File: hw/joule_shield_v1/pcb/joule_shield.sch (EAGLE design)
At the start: 143 parts, among them J1 MF-CON-MICROUSB-RIGHT, J4 USB_AUSB_A_SMT_RA, J5 JST-ZH5SMT_RA, J6 INTEL_JOULE_J6, J7 INTEL_JOULE_J7, J8 DM3ATDM3AT, Q1 NFETEMT3F, Q2 NFETEMT3F, Q3 NFETEMT3F, Q4 NFETEMT3F, Q5 NFETEMT3F, SW1 MF-SW-TACT-4.2MM, SW2 MF-SW-TACT-4.2MM, SW3 MF-SW-TACT-4.2MM, U1 BQ25892PWQFN-24, U10 FT231XQFN-20, U2 FAN8623WLCSP16, U3 TPS63201PVSON-14, U4 TLV62084PWSON-8, U5 TPS2553PWSON-6, U6 TPS2553PWSON-6, U7 SINGLE-BIT_BUS_TRANSCEIVER, U8 SINGLE-BIT_BUS_TRANSCEIVER, U9 SN74AVCA406L

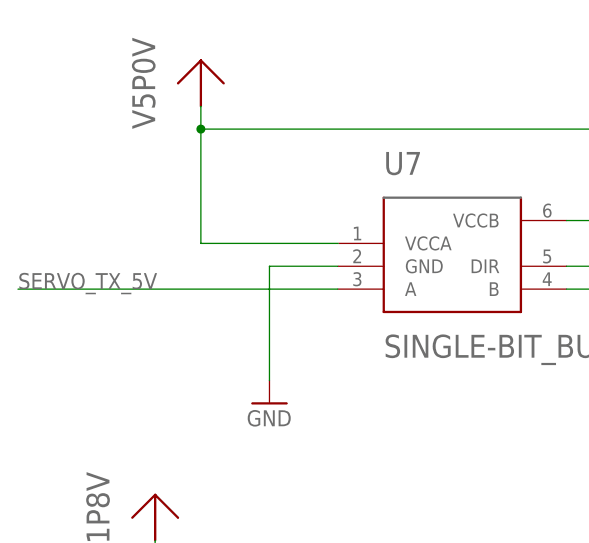
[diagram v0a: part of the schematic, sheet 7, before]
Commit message: joule shield: Do grounds for things up through the SD level converter.
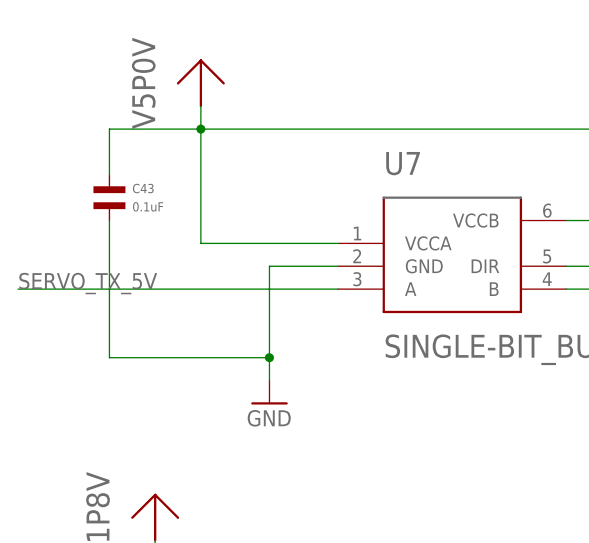
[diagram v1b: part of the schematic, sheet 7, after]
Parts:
- added C43: 0.1uF, mf_passives:CAPACITOR_NP_0603
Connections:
- net GND: now also C43.P$2
- net V5P0V: now also C43.P$1
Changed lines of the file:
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@@
 <part name="U$47" library="joule_shield" deviceset="VSYS" device=""/>
 <part name="U$13" library="joule_shield" deviceset="VSYS" device=""/>
+<part name="C43" library="mf_passives" deviceset="CAPACITOR_NP" device="_0603" value="0.1uF">
+<attribute name="MPN" value="MF-CAP-0603-0.1uF"/>
+</part>
 </parts>
 <sheets>
@@
 <instance part="C29" gate="G$1" x="25.4" y="27.94"/>
 <instance part="U$26" gate="G$1" x="96.52" y="91.44"/>
+<instance part="C43" gate="G$1" x="27.94" y="81.28"/>
 </instances>
 <busses>
@@
 <pinref part="U7" gate="G$1" pin="DIR"/>
 <wire x1="83.82" y1="73.66" x2="78.74" y2="73.66" width="0.1524" layer="91"/>
+<wire x1="38.1" y1="88.9" x2="27.94" y2="88.9" width="0.1524" layer="91"/>
+<pinref part="C43" gate="G$1" pin="P$1"/>
+<wire x1="27.94" y1="88.9" x2="27.94" y2="83.82" width="0.1524" layer="91"/>
 </segment>
 <segment>
@@
 <segment>
 <pinref part="GND24" gate="1" pin="GND"/>
-<wire x1="45.72" y1="60.96" x2="45.72" y2="73.66" width="0.1524" layer="91"/>
+<wire x1="45.72" y1="60.96" x2="45.72" y2="63.5" width="0.1524" layer="91"/>
 <pinref part="U7" gate="G$1" pin="GND"/>
+<wire x1="45.72" y1="63.5" x2="45.72" y2="73.66" width="0.1524" layer="91"/>
 <wire x1="45.72" y1="73.66" x2="53.34" y2="73.66" width="0.1524" layer="91"/>
-</segment>
-<segment>
+<pinref part="C43" gate="G$1" pin="P$2"/>
+<wire x1="27.94" y1="78.74" x2="27.94" y2="63.5" width="0.1524" layer="91"/>
+<wire x1="27.94" y1="63.5" x2="45.72" y2="63.5" width="0.1524" layer="91"/>
+<junction x="45.72" y="63.5"/>
+</segment>
+<segment>

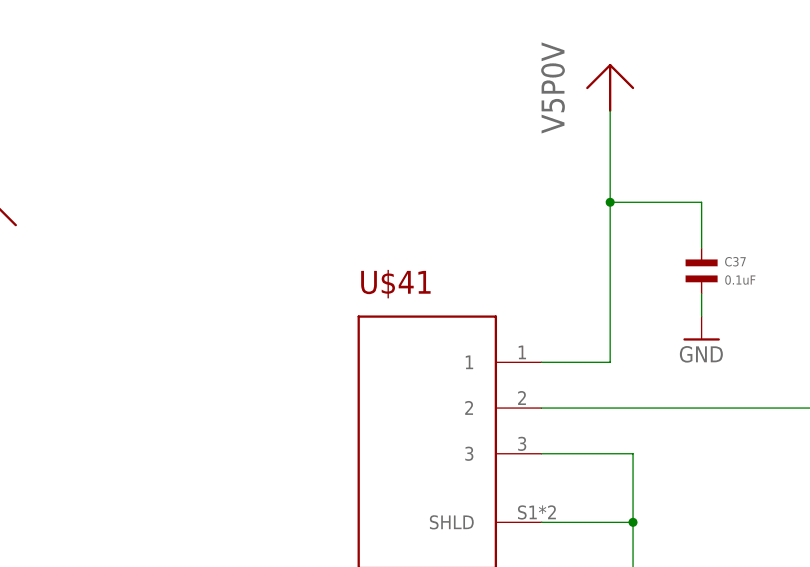
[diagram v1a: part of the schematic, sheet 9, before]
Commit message: joule shield: Get part numbers and populate attributes in for all parts.
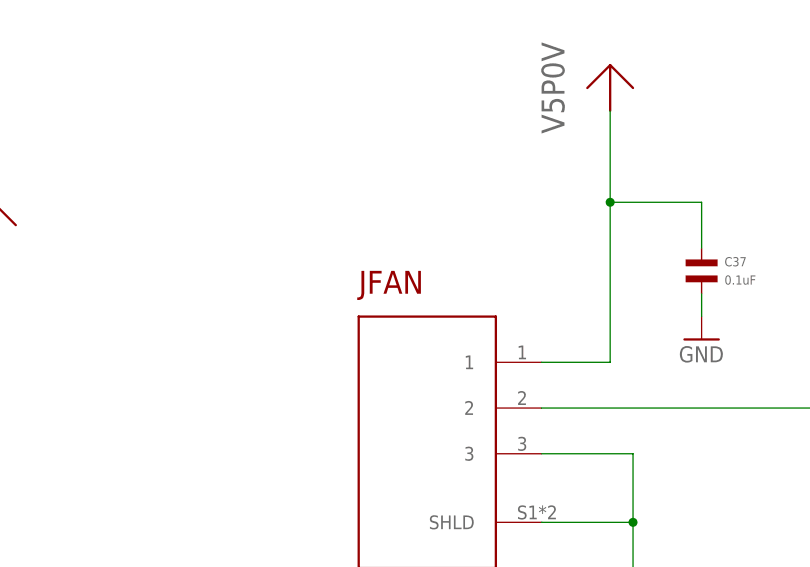
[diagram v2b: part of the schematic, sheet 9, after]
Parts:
- D2, D3, D4, D5, D6, D7, F1, J6, J7, JD1, JRTC, L1, L2, L3, L4, Q1, Q2, Q3, Q4, Q5, U1, U2, U3, U4, U5, U6, U7, U8: POPULATE (none) -> 1
- FB1, FB2, FB3: DPN (none) -> 490-5203-1-ND; MF (none) -> Murata; MPN (none) -> BLM15PD121SN1D; POPULATE (none) -> 1
- J4: DPN (none) -> 609-4413-ND; MF (none) -> Amphenol; MPN (none) -> 87583-2010BLF; POPULATE (none) -> 1
- J5: DPN (none) -> 455-1696-1-ND; MF (none) -> JST; MPN (none) -> S5B-ZR-SM4A-TF(LF)(SN); POPULATE (none) -> 1
- J8: DPN (none) -> HR1964CT-ND; MF (none) -> Hirose; MPN (none) -> DM3AT-SF-PEJM5; POPULATE (none) -> 1
- JFAN: DPN (none) -> A101008CT-ND; MF (none) -> TE Connectivity; MPN (none) -> 292228-3; POPULATE (none) -> 1
- TP1, TP2, TP3, U$48, U$49, U$50, U$51, U$52, U$53, U$54, U$55: POPULATE (none) -> 0
- U10: DPN (none) -> 768-1128-1-ND; MF (none) -> FTDI; MPN (none) -> FT231XQ-R; POPULATE (none) -> 1
- U9: DPN (none) -> 296-21023-1-ND; MF (none) -> Texas Instruments; MPN (none) -> SN74AVCA406LZXYR; POPULATE (none) -> 1
- renumbered U$41 to JFAN

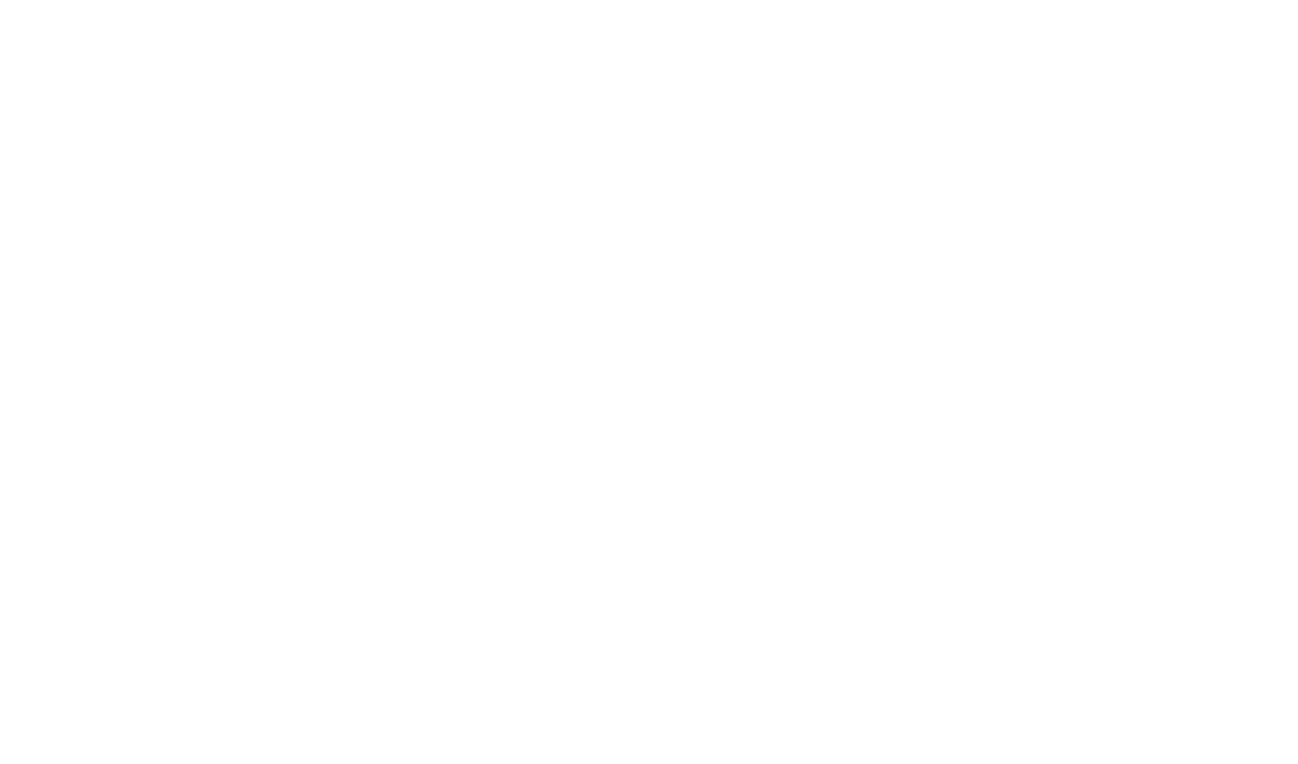
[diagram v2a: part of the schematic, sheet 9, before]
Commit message: joule_shield: Include and place an I2C EEPROM.
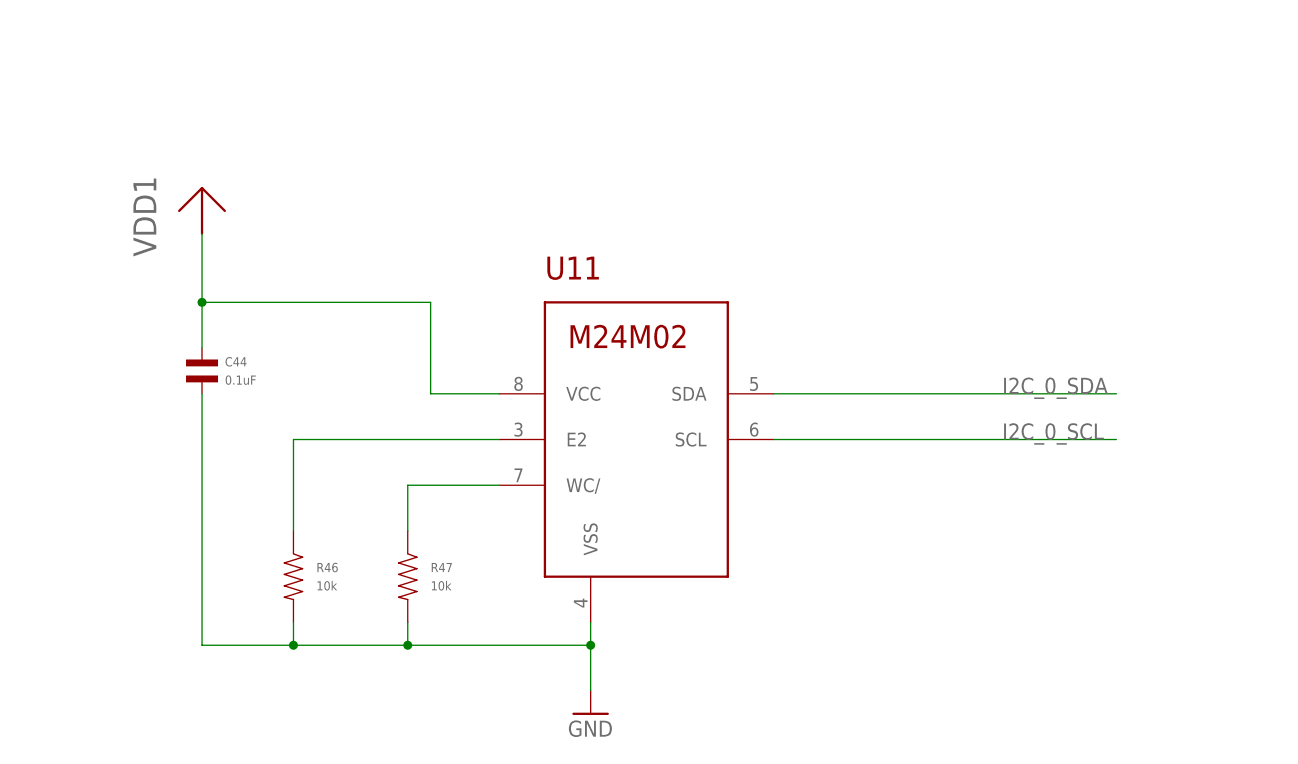
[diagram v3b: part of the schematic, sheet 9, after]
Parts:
- added C44: 0.1uF, mf_passives:CAPACITOR_NP_0603
- added R46, R47: 10k, mf_passives:RESISTOR_0603
- added U11: M24M02SO8N, joule_shield:M24M02SO8N
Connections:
- new net N$22: R46.P$1, U11.E2
- new net N$32: R47.P$1, U11.WC/
- net GND: now also C44.P$2, R46.P$2, R47.P$2, U11.VSS
- net I2C_0_SCL: now also U11.SCL
- net I2C_0_SDA: now also U11.SDA
- net VDD1: now also C44.P$1, U11.VCC
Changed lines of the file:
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@@
 <attribute name="MPN" value="MF-CAP-0603-0.1uF"/>
+</part>
+<part name="U11" library="joule_shield" deviceset="M24M02" device="SO8N"/>
+<part name="GND54" library="supply1" deviceset="GND" device=""/>
+<part name="U$41" library="joule_shield" deviceset="VDD1" device=""/>
+<part name="C44" library="mf_passives" deviceset="CAPACITOR_NP" device="_0603" value="0.1uF">
+<attribute name="MPN" value="MF-CAP-0603-0.1uF"/>
+</part>
+<part name="R46" library="mf_passives" deviceset="RESISTOR" device="_0603" value="10k">
+<attribute name="MPN" value="MF-RES-0603-10K"/>
+</part>
+<part name="R47" library="mf_passives" deviceset="RESISTOR" device="_0603" value="10k">
+<attribute name="MPN" value="MF-RES-0603-10K"/>
 </part>
 </parts>
@@
 </instance>
 <instance part="GND50" gate="1" x="154.94" y="101.6"/>
+<instance part="U11" gate="G$1" x="73.66" y="-38.1"/>
+<instance part="GND54" gate="1" x="68.58" y="-68.58"/>
+<instance part="U$41" gate="G$1" x="25.4" y="-15.24"/>
+<instance part="C44" gate="G$1" x="25.4" y="-30.48"/>
+<instance part="R46" gate="G$1" x="35.56" y="-53.34"/>
+<instance part="R47" gate="G$1" x="48.26" y="-53.34"/>
 </instances>
 <busses>
@@
 <junction x="154.94" y="106.68"/>
 </segment>
+<segment>
+<pinref part="GND54" gate="1" pin="GND"/>
+<pinref part="U11" gate="G$1" pin="VSS"/>
+<wire x1="68.58" y1="-66.04" x2="68.58" y2="-60.96" width="0.1524" layer="91"/>
+<pinref part="C44" gate="G$1" pin="P$2"/>
+<wire x1="68.58" y1="-60.96" x2="68.58" y2="-58.42" width="0.1524" layer="91"/>
+<wire x1="25.4" y1="-33.02" x2="25.4" y2="-60.96" width="0.1524" layer="91"/>
+<wire x1="25.4" y1="-60.96" x2="35.56" y2="-60.96" width="0.1524" layer="91"/>
+<junction x="68.58" y="-60.96"/>
+<pinref part="R46" gate="G$1" pin="P$2"/>
+<wire x1="35.56" y1="-60.96" x2="48.26" y2="-60.96" width="0.1524" layer="91"/>
+<wire x1="48.26" y1="-60.96" x2="68.58" y2="-60.96" width="0.1524" layer="91"/>
+<wire x1="35.56" y1="-60.96" x2="35.56" y2="-58.42" width="0.1524" layer="91"/>
+<junction x="35.56" y="-60.96"/>
+<pinref part="R47" gate="G$1" pin="P$2"/>
+<wire x1="48.26" y1="-60.96" x2="48.26" y2="-58.42" width="0.1524" layer="91"/>
+<junction x="48.26" y="-60.96"/>
+</segment>
 </net>
 <net name="VRTC" class="0">
@@
 <wire x1="144.78" y1="144.78" x2="144.78" y2="139.7" width="0.1524" layer="91"/>
 </segment>
+<segment>
+<pinref part="U$41" gate="G$1" pin="VDD1"/>
+<pinref part="C44" gate="G$1" pin="P$1"/>
+<wire x1="25.4" y1="-15.24" x2="25.4" y2="-22.86" width="0.1524" layer="91"/>
+<wire x1="25.4" y1="-22.86" x2="25.4" y2="-27.94" width="0.1524" layer="91"/>
+<wire x1="25.4" y1="-22.86" x2="50.8" y2="-22.86" width="0.1524" layer="91"/>
+<wire x1="50.8" y1="-22.86" x2="50.8" y2="-33.02" width="0.1524" layer="91"/>
+<junction x="25.4" y="-22.86"/>
+<pinref part="U11" gate="G$1" pin="VCC"/>
+<wire x1="50.8" y1="-33.02" x2="58.42" y2="-33.02" width="0.1524" layer="91"/>
+</segment>
 </net>
 <net name="N$52" class="0">
@@
 </segment>
 </net>
+<net name="N$22" class="0">
+<segment>
+<pinref part="R46" gate="G$1" pin="P$1"/>
+<wire x1="35.56" y1="-48.26" x2="35.56" y2="-38.1" width="0.1524" layer="91"/>
+<pinref part="U11" gate="G$1" pin="E2"/>
+<wire x1="35.56" y1="-38.1" x2="58.42" y2="-38.1" width="0.1524" layer="91"/>
+</segment>
+</net>
+<net name="N$32" class="0">
+<segment>
+<pinref part="R47" gate="G$1" pin="P$1"/>
+<wire x1="48.26" y1="-48.26" x2="48.26" y2="-43.18" width="0.1524" layer="91"/>
+<pinref part="U11" gate="G$1" pin="WC/"/>
+<wire x1="48.26" y1="-43.18" x2="58.42" y2="-43.18" width="0.1524" layer="91"/>
+</segment>
+</net>
+<net name="I2C_0_SDA" class="0">
+<segment>
+<pinref part="U11" gate="G$1" pin="SDA"/>
+<wire x1="88.9" y1="-33.02" x2="127" y2="-33.02" width="0.1524" layer="91"/>
+<label x="114.3" y="-33.02" size="1.778" layer="95"/>
+</segment>
+</net>
+<net name="I2C_0_SCL" class="0">
+<segment>
+<pinref part="U11" gate="G$1" pin="SCL"/>
+<wire x1="88.9" y1="-38.1" x2="127" y2="-38.1" width="0.1524" layer="91"/>
+<label x="114.3" y="-38.1" size="1.778" layer="95"/>
+</segment>
+</net>

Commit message: joule shield snapshot
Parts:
- removed C13, C14, C21: 10uF, mf_passives:CAPACITOR_NP_0603
- removed C15, C22: 1uF, mf_passives:CAPACITOR_NP_0603
- removed C16, C44: 0.1uF, mf_passives:CAPACITOR_NP_0603
- removed L3, L4: 1uH, joule_shield:INDUCTORSPM4012
- removed R13, R18: 0, mf_passives:RESISTOR_0603
- removed R14, R15: 100k, mf_passives:RESISTOR_0603
- removed R16: 110.0k 1%, mf_passives:RESISTOR_0603
- removed R17: 36.5k 1%, mf_passives:RESISTOR_0603
- removed R46, R47: 10k, mf_passives:RESISTOR_0603
- removed TP2, TP3: TPSQB1,27, testpad:TPSQB1,27
- removed U11: M24M02SO8N, joule_shield:M24M02SO8N
- removed U3: TPS63201PVSON-14, joule_shield:TPS63201PVSON-14
- removed U4: TLV62084PWSON-8, joule_shield:TLV62084PWSON-8
- added FB4, FB5: FERRITE_BEAD, joule_shield:FERRITE_BEAD
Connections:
- removed net N$16: L3.1, U3.L1
- removed net N$17: L3.2, U3.L2
- removed net N$19: C16.P$1, U3.VINA
- removed net N$20: R13.P$2, U3.EN
- removed net N$21: R14.P$2, TP2.TP, U3.PG
- removed net N$22: R46.P$1, U11.E2
- removed net N$23: L4.1, U4.SW
- removed net N$25: R15.P$2, TP3.TP, U4.PG
- removed net N$26: R16.P$2, R17.P$1, U4.FB
- removed net N$27: R18.P$2, U4.EN
- removed net N$32: R47.P$1, U11.WC/
- net GND: no longer C13.P$2, C14.P$2, C15.P$2, C16.P$2, C21.P$2, C22.P$2, C44.P$2, R17.P$2, R46.P$2, R47.P$2, U11.VSS, U3.GND, U3.PGND, U3.PS/SYNC, U4.GND
- net I2C_0_SCL: no longer U11.SCL
- net I2C_0_SDA: no longer U11.SDA
- net V1P8V: now also FB4.P$2; no longer L4.2, R15.P$1, R16.P$1, U4.VOS
- net V3P3V: now also FB5.P$2; no longer R14.P$1, U3.FB, U3.VOUT
- net VDD1: now also FB4.P$1; no longer C44.P$1, R18.P$1, U11.VCC
- net VDD3: now also FB5.P$1; no longer R13.P$1
- net VSYS: no longer C13.P$1, C14.P$1, C15.P$1, C21.P$1, C22.P$1, U3.VIN, U4.VIN
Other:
- moved on the sheet: C17, C18, C19, C20, C23, C24, C25
